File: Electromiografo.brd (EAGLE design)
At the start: 101.3 x 76.2 mm, 41 parts, among them IC1 ESP32-S3-WROOM-1-N16R8, IC10 LMV321IDBVRG4, IC2 MCP73831T-2DCI_OT, IC3 741G3157DBVR, IC4 LP38692MP-3.3_NOPB, IC5 REF2033AIDDCT, IC6 LMV321IDBVRG4, IC7 LMV321IDBVRG4, IC8 LMV321IDBVRG4, IC9 AD8223ARMZ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

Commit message: modificacion pulsadores
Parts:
- IC9: device SamacSys_Parts:SOP65P490X110-8N -> SamacSys_Parts:SOP65P490X110-8N@1
- S1, S2: value PTS125SM73SMTR21M_LFS -> B3U-1000PM; device SamacSys_Parts:PTS125SM73SMTR21MLFS -> SamacSys_Parts:B3U1000PM
- moved JP1 36.8 mm to (95.2, 47.0)
- moved IC1 31.9 mm to (55.9, 59.7), turned to 0 degrees
- moved S1 28.1 mm to (31.8, 55.9), turned to 0 degrees
- moved C3 23.7 mm to (39.4, 53.3)
- moved C11 22.5 mm to (40.6, 57.1)
- moved R1 21.7 mm to (72.4, 41.9), turned to 0 degrees
- moved C2 18.2 mm to (40.6, 59.7)
- moved R2 17.7 mm to (40.6, 73.7), turned to 0 degrees
- moved C1 16.3 mm to (40.6, 68.6)
- moved S2 6.84 mm to (33.0, 64.8)
- moved R12 1.27 mm to (36.8, 44.5)
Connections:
- net GND: now also S1.1, S2.2; no longer S1.D1, S2.B1
- net N$1: now also S1.2; no longer S1.B1
- net N$2: now also S2.1; no longer S2.D1
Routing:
- net GND: track 0.00 -> 12.8 mm
- net N$17: track 10.0 -> 8.74 mm
- net OUTADC: track 5.52 -> 4.25 mm

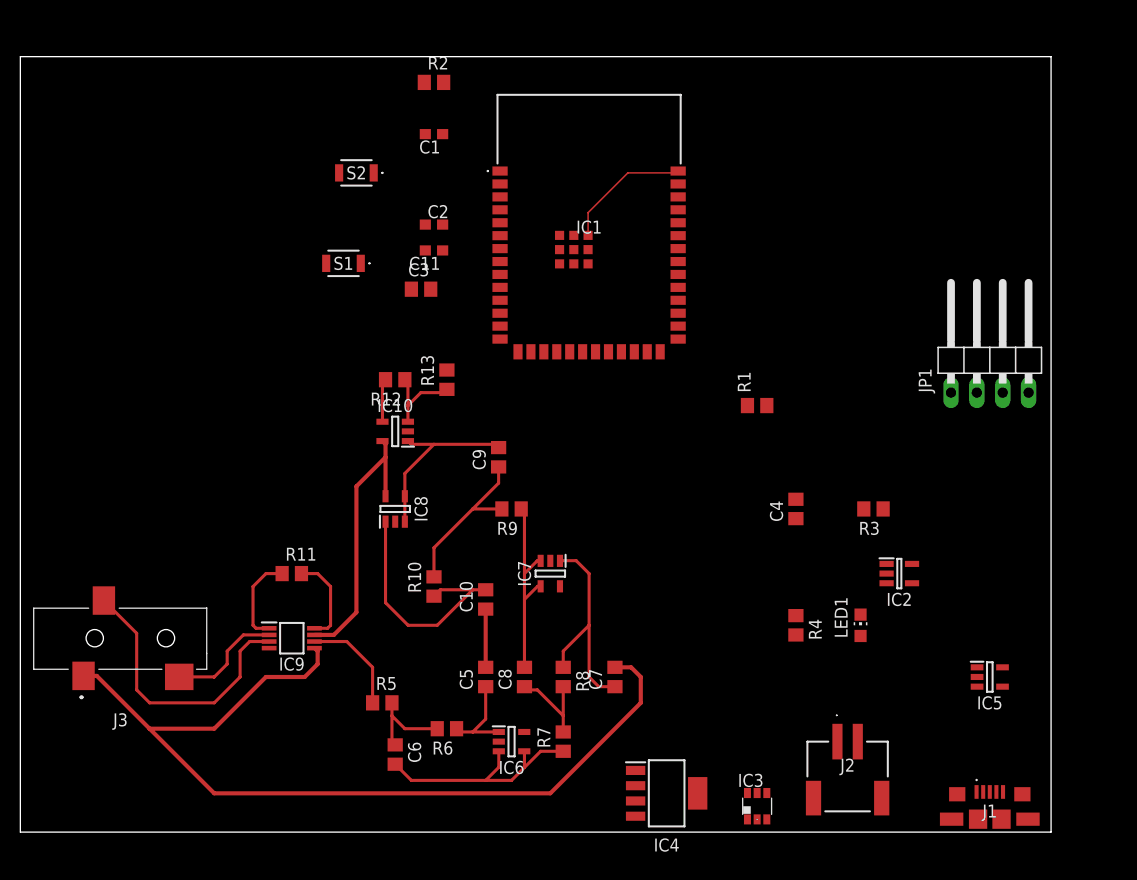
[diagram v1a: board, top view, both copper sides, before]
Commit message: Se rutearon las pistas de alimentacion del pcb
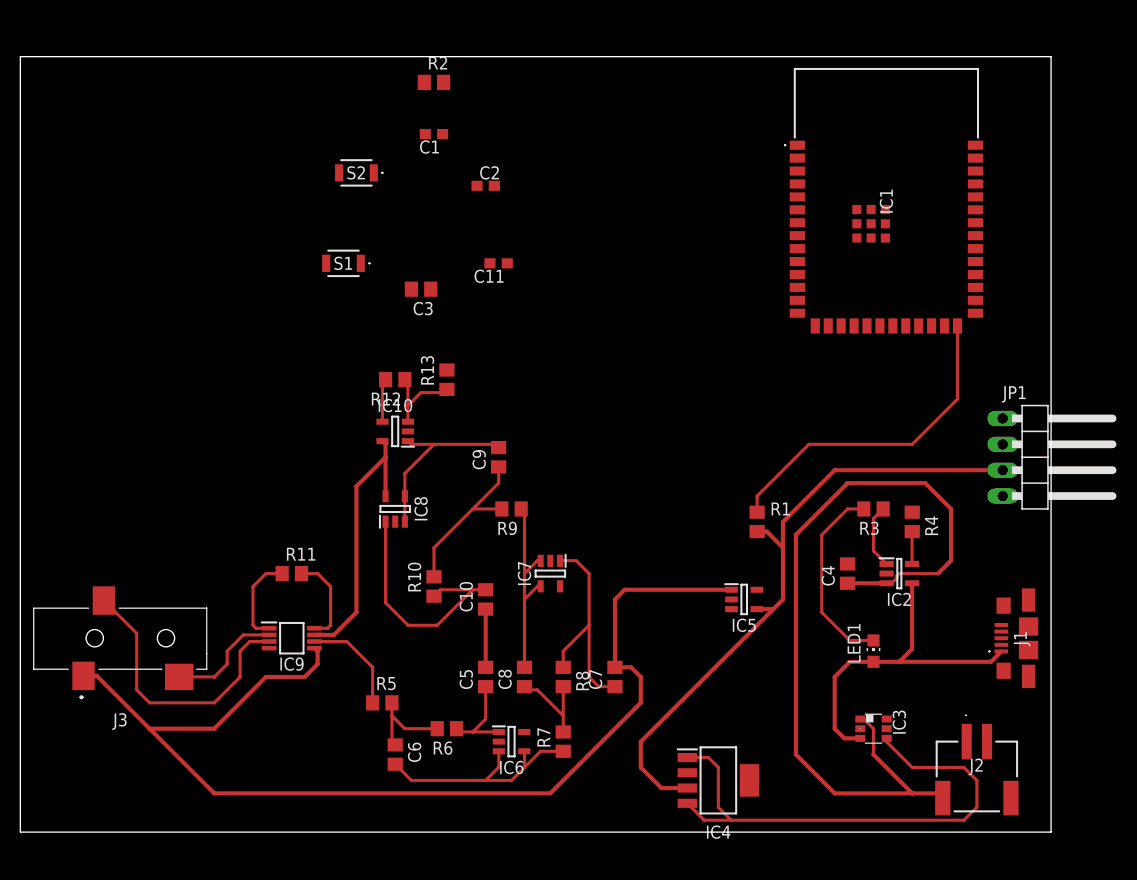
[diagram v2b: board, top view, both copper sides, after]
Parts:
- moved IC1 29.3 mm to (85.1, 62.2)
- moved IC5 25.3 mm to (71.1, 22.9)
- moved J1 18.2 mm to (99.1, 19.1), turned to 90 degrees
- moved R4 15.3 mm to (87.6, 30.5)
- moved IC3 13.7 mm to (83.8, 10.2), turned to 270 degrees
- moved J2 12.7 mm to (94.0, 8.89)
- moved R1 11.4 mm to (72.4, 30.5), turned to 270 degrees
- moved JP1 11.4 mm to (100.3, 36.8), turned to 270 degrees
- moved C4 8.13 mm to (81.3, 25.4)
- moved C11 6.48 mm to (47.0, 55.9)
- moved C2 6.35 mm to (45.7, 63.5)
- moved IC4 5.24 mm to (68.6, 5.08)
- moved LED1 2.84 mm to (83.8, 17.8)
- turned C3 to 180 degrees
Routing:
- net +BAT: track 0.00 -> 82.1 mm
- net +3V3: track 27.0 -> 90.8 mm
- net N$26: track 0.00 -> 52.2 mm
- net +5V: track 0.00 -> 33.6 mm
- net N$1: track 0.00 -> 32.4 mm
- net N$14: track 0.00 -> 19.0 mm
- net VSS: track 95.3 -> 113.8 mm
- net GND: track 12.8 -> 0.25 mm
- net N$24: track 0.00 -> 6.33 mm
- net N$25: track 0.00 -> 3.19 mm

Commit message: Se termino version uno del pcb
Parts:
- moved JP1 84.7 mm to (20.3, 64.8), turned to 0 degrees
- moved C3 62.0 mm to (96.5, 29.2), turned to 0 degrees
- moved C1 47.1 mm to (62.2, 26.7), turned to 0 degrees
- moved C11 32.5 mm to (67.3, 30.5), turned to 270 degrees
- moved R2 24.4 mm to (52.1, 52.1), turned to 270 degrees
- moved S2 16.7 mm to (49.5, 62.2), turned to 270 degrees
- moved IC1 16.3 mm to (72.4, 52.1)
- moved C2 15.3 mm to (55.9, 52.1), turned to 90 degrees
- moved S1 8.13 mm to (36.8, 62.2), turned to 90 degrees
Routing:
- net +3V3: track 90.8 -> 214.1 mm, vias 0 -> 4
- net N$1: track 32.4 -> 72.0 mm, vias 0 -> 2
- net OUTADC: track 4.25 -> 42.9 mm
- net N$2: track 0.00 -> 23.8 mm
- net +5V: track 33.6 -> 48.3 mm
- added copper zone on layer 1, net GND
- added copper zone on layer 16, net GND
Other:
- board size 101.3 x 76.2 mm -> 101.3 x 66 mm

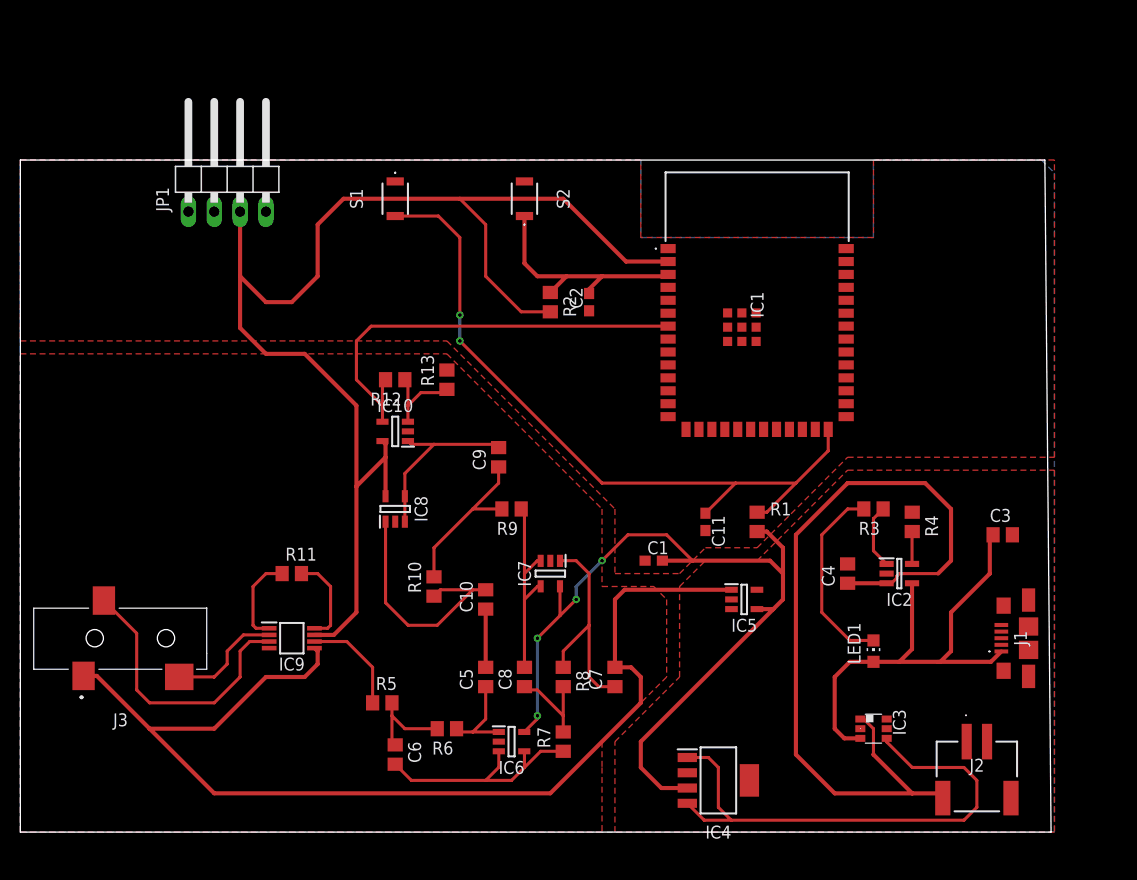
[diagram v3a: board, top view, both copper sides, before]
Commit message: corregido el switche
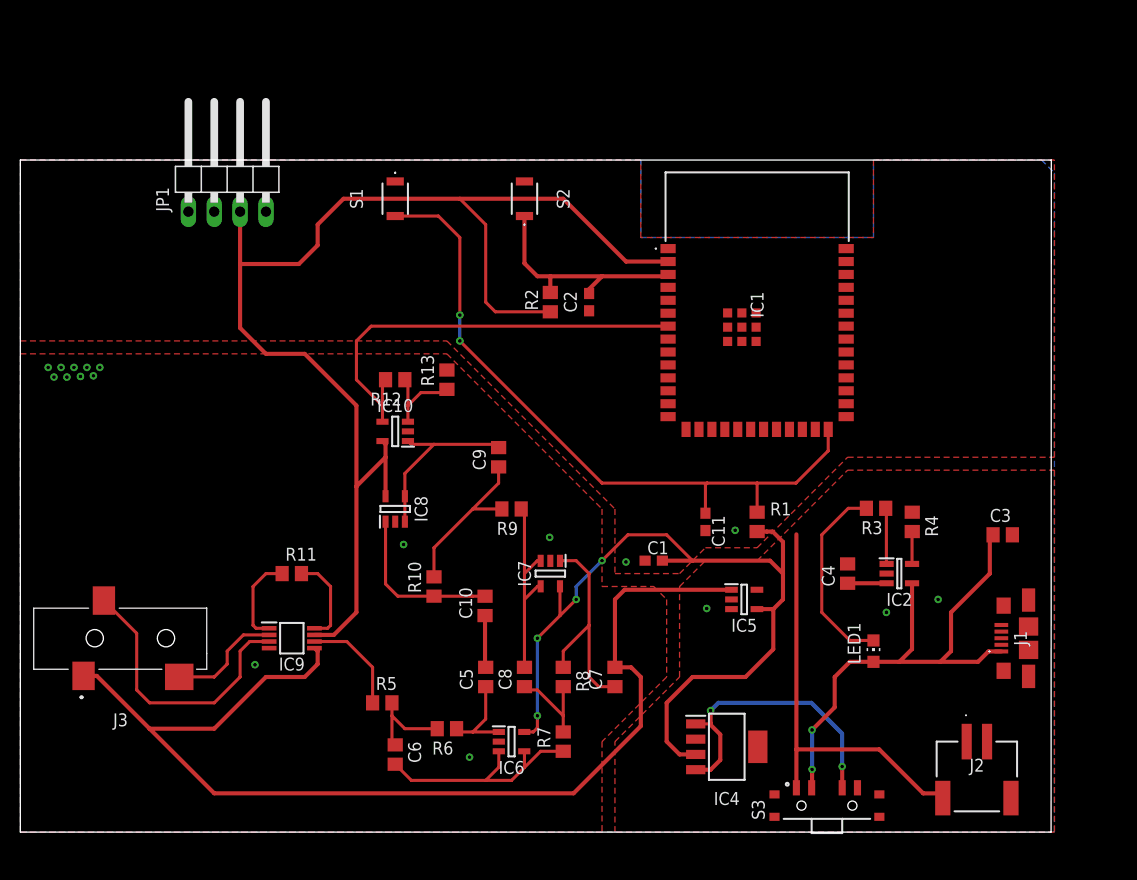
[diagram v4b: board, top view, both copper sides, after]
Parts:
- removed IC3: 741G3157DBVR, 74xx-little-us:DBV_R-PDSO-G6
- added S3: PCM13SMTR, PCM13SMTR:SW_PCM13SMTR
- moved IC4 3.40 mm to (69.4, 8.38)
- moved C10 0.64 mm to (45.7, 22.2)
- moved R3 0.26 mm to (84.1, 31.8)
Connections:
- removed net VCC: IC3.5
- net +5V: now also S3.2; no longer IC3.3
- net +BAT: now also S3.1; no longer IC3.1
- net GND: no longer IC3.2
- net N$26: now also S3.3; no longer IC3.4
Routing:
- net +BAT: track 82.1 -> 45.6 mm
- net N$26: track 52.2 -> 29.3 mm, vias 0 -> 2
- net N$37: track 24.2 -> 16.4 mm
- net +3V3: track 214.1 -> 209.5 mm
- net +5V: track 48.3 -> 52.1 mm, vias 0 -> 2
- net N$1: track 72.0 -> 68.7 mm
- net N$24: track 6.33 -> 5.50 mm
- net VSS: track 113.8 -> 114.5 mm
- net N$2: track 23.8 -> 23.2 mm
- net GND: vias 0 -> 18
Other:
- outline, holes or cut-outs redrawn

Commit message: Modificaciones esquematico, version 2 de pcb
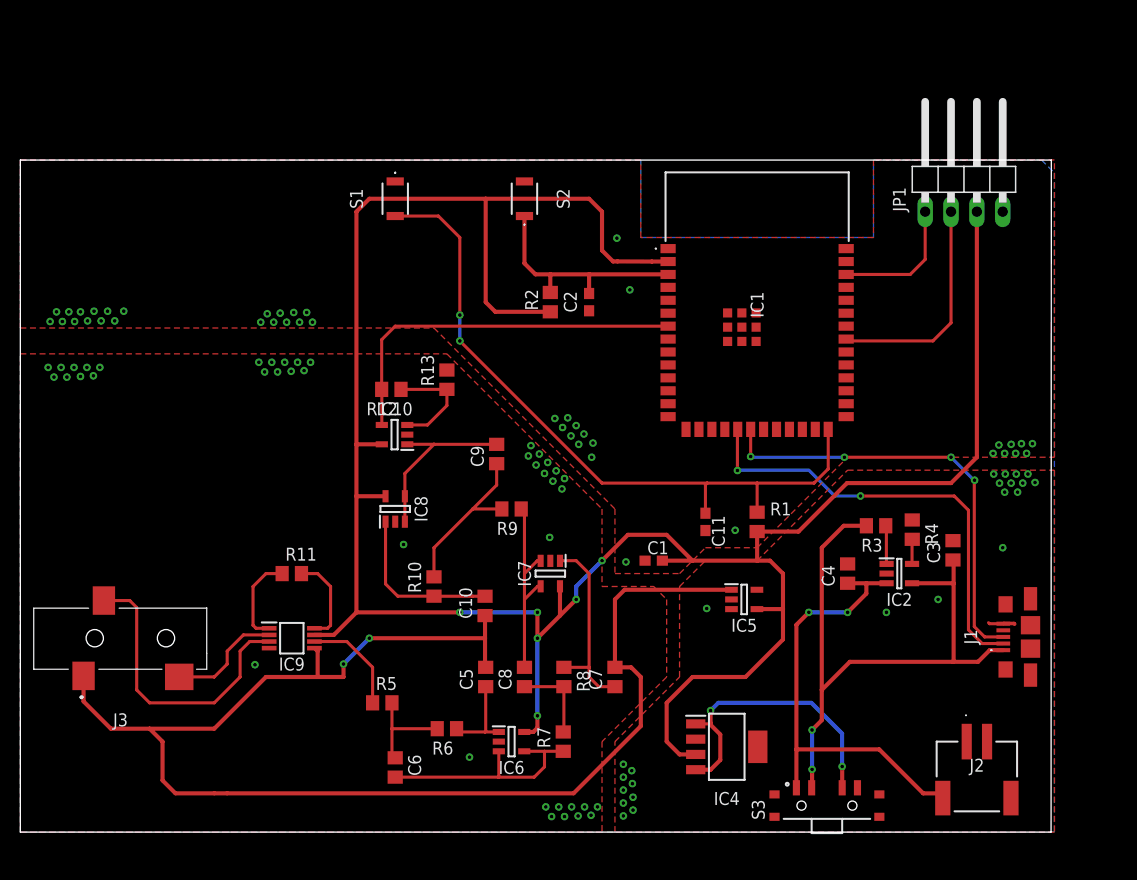
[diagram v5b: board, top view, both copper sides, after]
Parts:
- removed LED1: (no value), PulseOximeterECG_AU:CHIP-LED0805
- moved JP1 72.4 mm to (92.7, 64.8)
- moved C3 5.12 mm to (91.6, 27.7), turned to 90 degrees
- moved R3 1.71 mm to (84.1, 30.1)
- moved C6 1.27 mm to (36.8, 6.35)
- moved R12 1.03 mm to (36.4, 43.5)
- moved R4 0.76 mm to (87.6, 29.7)
- moved C9 0.37 mm to (46.8, 37.1)
- moved IC10 0.32 mm to (36.8, 39.1)
- moved J1 0.23 mm to (99.3, 19.2)
- moved R8 0.06 mm to (53.4, 15.2)
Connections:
- net N$12 renamed RX
- net N$15 renamed TX
- net N$2 renamed RESET
- net N$4 renamed DAC1
- net N$6 renamed DAC2
- net N$7 renamed TOUCHPAD1
- net N$8 renamed TOUCHPAD2
- net N$9 renamed TOUCHPAD3
- removed net N$10: IC1.23
- removed net N$11: IC1.24
- removed net N$14: LED1.C, R3.2
- removed net N$16: IC1.38
- removed net N$21: JP1.2
- removed net N$22: JP1.1
- new net SCL: IC1.38, JP1.1
- net +5V: now also R3.2; no longer LED1.A
- net D+: now also IC1.20
- net D-: now also IC1.19
- net SDA: now also JP1.2
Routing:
- net D-: track 0.00 -> 44.2 mm, vias 0 -> 2
- net D+: track 0.00 -> 43.3 mm, vias 0 -> 4
- net +3V3: track 209.5 -> 251.5 mm, vias 4 -> 6
- net VSS: track 114.5 -> 137.7 mm, vias 0 -> 2
- net SDA: track 0.00 -> 22.0 mm
- net N$14: track 19.3 -> 0.00 mm
- net SCL: track 0.00 -> 13.1 mm
- net +5V: track 52.1 -> 62.9 mm
- net OUTADC: track 42.9 -> 37.1 mm
- net GND: track 0.25 -> 4.07 mm, vias 18 -> 106
- net N$34: track 21.7 -> 19.0 mm
- net N$17: track 8.74 -> 11.2 mm
- net N$24: track 5.50 -> 3.78 mm
- net INA+: track 27.6 -> 29.1 mm
- net N$1: track 68.7 -> 69.7 mm
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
